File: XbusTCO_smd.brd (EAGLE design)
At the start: 54 x 70 mm, 80 parts, among them IC1 74HC4515D, IC2 PIC16F628P, IC3 MAX481CSA, IC4 78L05SMD, X1 1751264

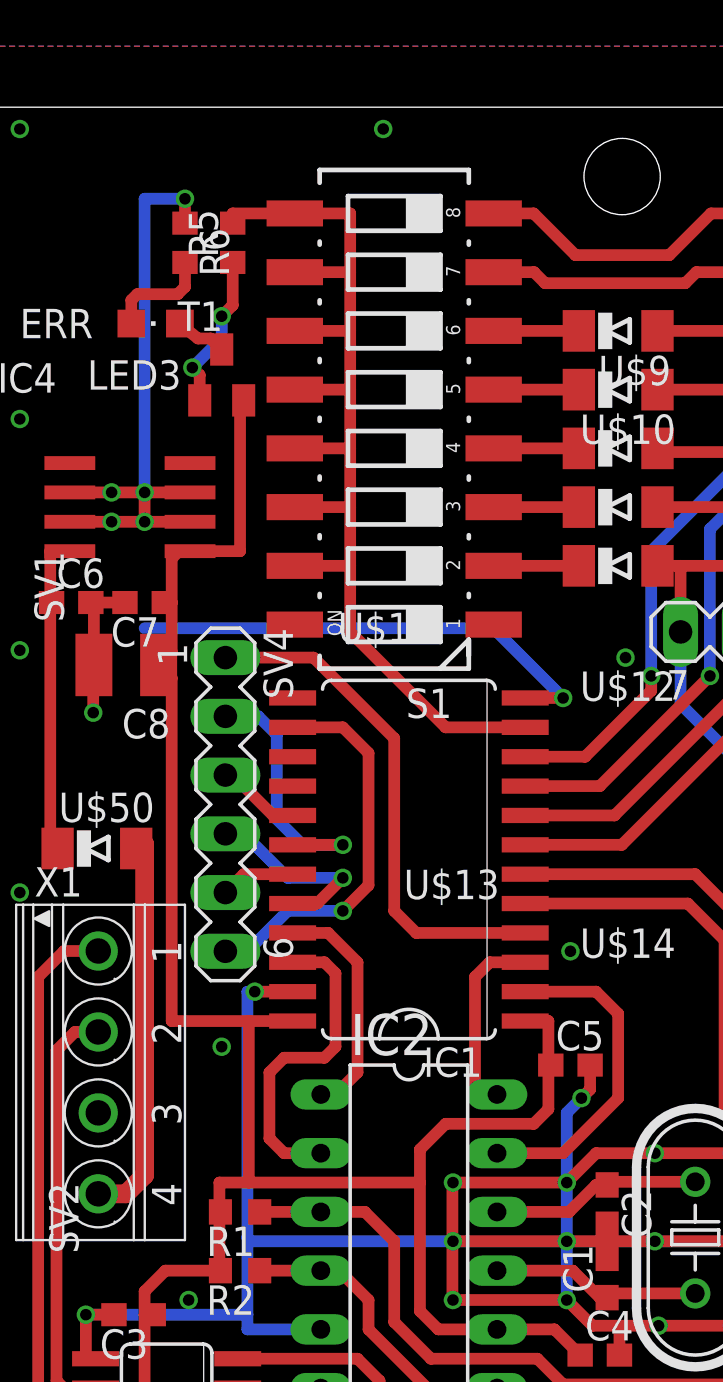
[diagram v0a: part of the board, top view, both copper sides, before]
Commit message: Updated DIL switch pinout.
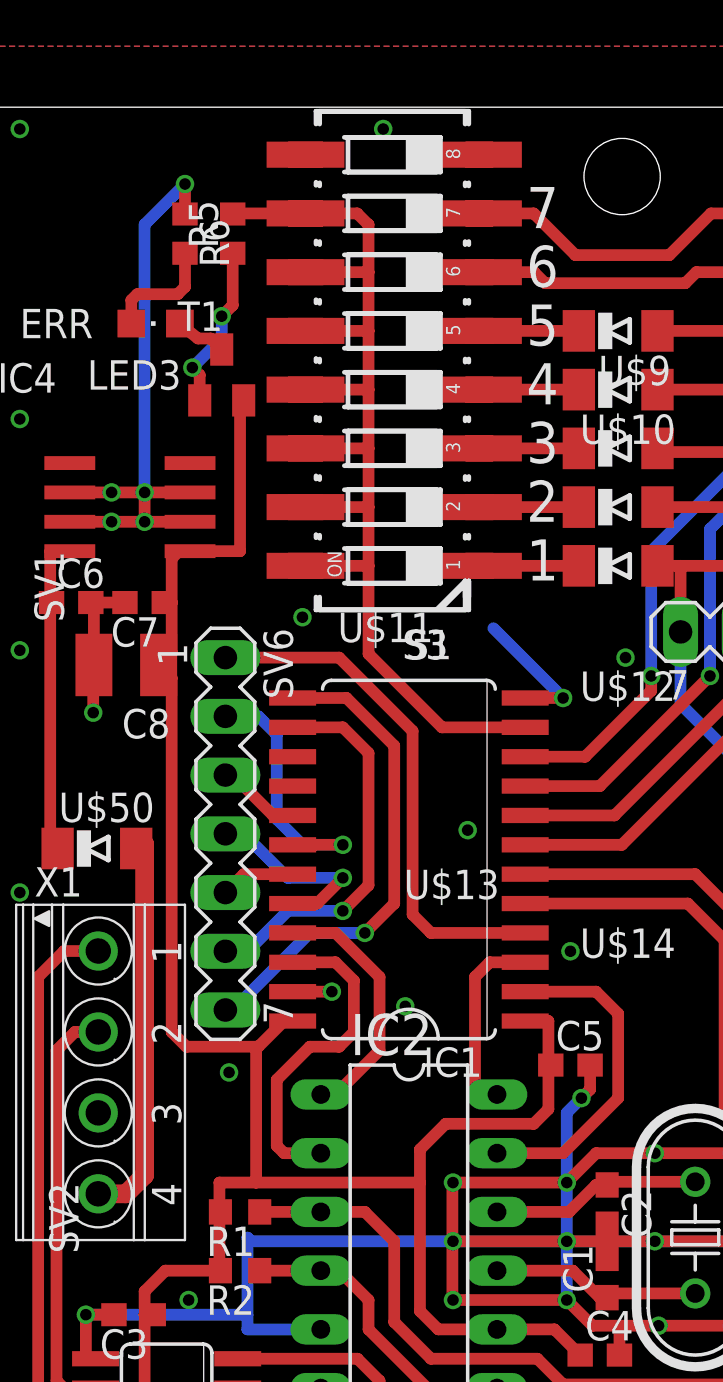
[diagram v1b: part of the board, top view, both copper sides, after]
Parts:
- removed SV4: (no value), con-lstb:MA06-1
- added S3: Farnel 1605476, switch-dil:CTS-219-08J
- added SV6: (no value), con-lstb:MA07-1
- moved S1 2.54 mm to (17.1, 59.1)
- moved R5 0.40 mm to (10.2, 64.5)
- moved R6 0.40 mm to (8.10, 64.5)
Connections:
- new net N$88: IC1.13, SV6.7
- net GND: now also S1.8, S1.9, S3.8, S3.9
- net N$30: now also S1.16, S3.10, S3.11, S3.12, S3.13, S3.14, S3.15, S3.16; no longer S1.9
- net N$31: now also S1.7, S3.7; no longer S1.8
- net N$32: now also S1.6, S3.6; no longer S1.7
- net N$33: now also S1.5, S3.5; no longer S1.6
- net N$34: now also S1.4, S3.4; no longer S1.5
- net N$35: now also S1.3, S3.3; no longer S1.4
- net N$36: now also S1.2, S3.2; no longer S1.3
- net N$37: now also S1.1, S3.1; no longer S1.2
- net N$82: now also SV6.1; no longer SV4.1
- net N$83: now also SV6.2; no longer SV4.2
- net N$84: now also SV6.3; no longer SV4.3
- net N$85: now also SV6.4; no longer SV4.4
- net N$86: now also SV6.5; no longer SV4.5
- net N$87: now also SV6.6; no longer SV4.6
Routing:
- net GND: track 172.1 -> 146.0 mm, vias 39 -> 42
- net N$88: track 0.00 -> 21.3 mm, vias 0 -> 1
- net N$30: track 47.2 -> 52.8 mm
- net N$32: track 12.5 -> 15.0 mm
- net N$37: track 3.68 -> 4.93 mm
- net N$36: track 3.68 -> 4.93 mm
- net N$35: track 3.68 -> 4.93 mm
- net N$34: track 3.68 -> 4.93 mm
- net N$33: track 3.68 -> 4.93 mm
- net N$31: track 13.6 -> 14.8 mm
- net N$5: track 10.1 -> 11.1 mm
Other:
- board text added: "1"
- board text added: "2"
- board text added: "3"
- board text added: "4"
- board text added: "5"
- board text added: "6"
- board text added: "7"

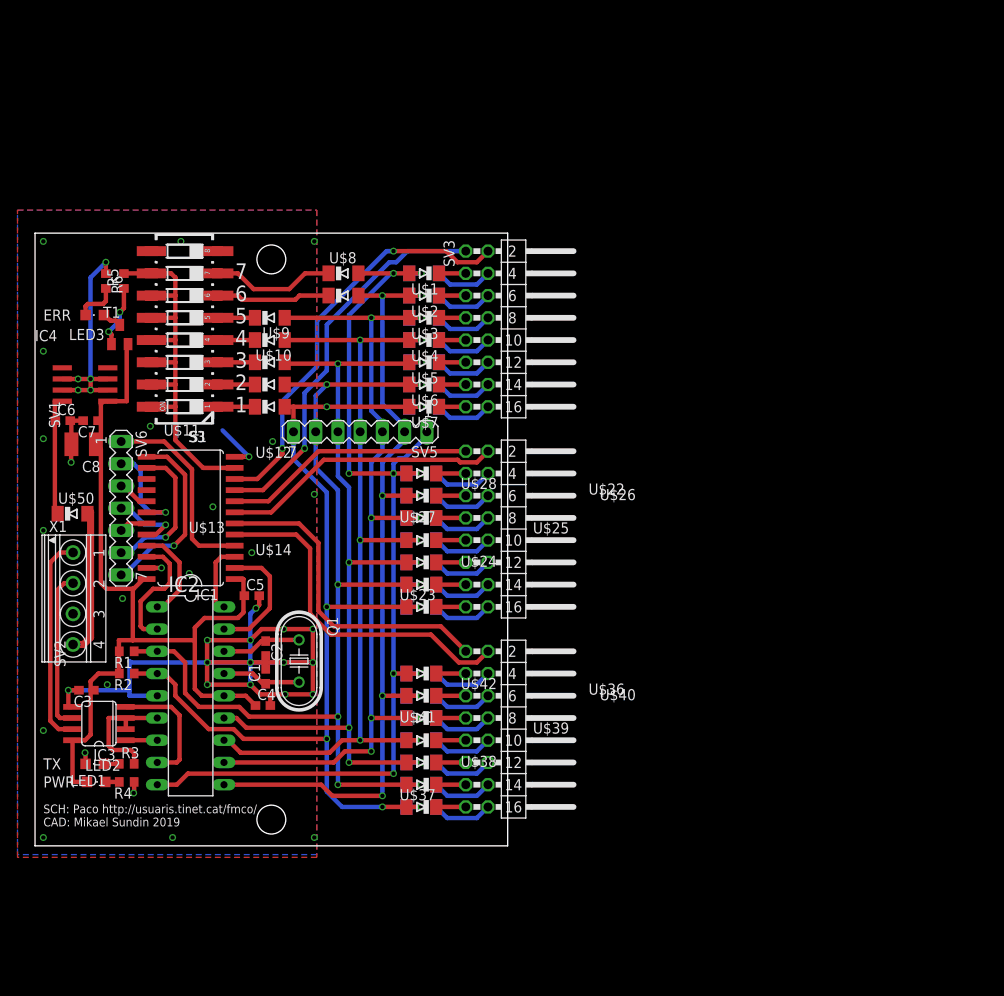
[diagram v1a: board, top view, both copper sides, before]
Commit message: Added 2 more connectors.
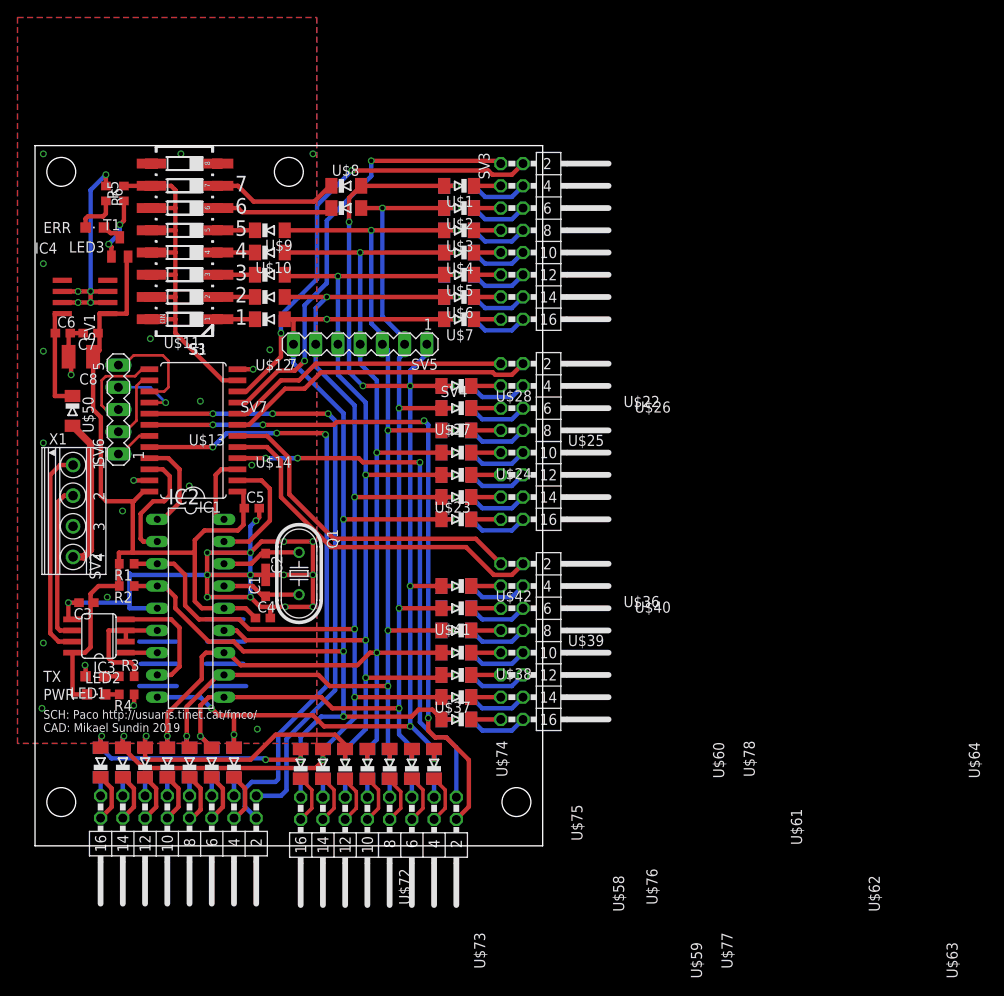
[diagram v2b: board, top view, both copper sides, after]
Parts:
- added SV4, SV7: (no value), con-lstb:MA08-2W
- added U$51, U$52, U$53, U$54, U$55, U$56, U$57, U$58, U$59, U$60, U$61, U$62, U$63, U$64, U$65, U$66, U$67, U$68, U$69, U$70, U$71, U$72, U$73, U$74, U$75, U$76, U$77, U$78: LL4148, LL4148:MINIMELF
- SV6: device con-lstb:MA07-1 -> con-lstb:MA05-1
- moved U$50 11.7 mm to (4.29, 49.7), turned to 270 degrees
- moved SV6 11.3 mm to (9.53, 49.8), turned to 90 degrees
- moved SV3 10.8 mm to (54.5, 69.1)
- moved U$17 10.8 mm to (48.5, 65.2)
- moved U$5 10.8 mm to (48.5, 65.2)
- moved SV1 10.8 mm to (54.5, 46.2)
- moved SV2 10.8 mm to (54.5, 23.3)
- moved U$1 10.8 mm to (48.5, 75.4)
- moved U$15 10.8 mm to (48.5, 60.2)
- moved U$16 10.8 mm to (48.5, 62.7)
- moved U$18 10.8 mm to (48.5, 67.8)
- moved U$19 10.8 mm to (48.5, 70.3)
- moved U$21 10.8 mm to (48.5, 75.4)
- moved U$22 10.8 mm to (48.1, 52.5)
- moved U$23 10.8 mm to (48.1, 50.0)
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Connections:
- new net N$100: SV4.7, U$53.C
- new net N$101: SV4.9, U$54.C
- new net N$102: SV4.11, U$55.C
- new net N$103: SV4.13, U$56.C
- new net N$104: SV4.15, U$57.C
- new net N$105: SV4.16, U$58.C
- new net N$106: SV4.14, U$59.C
- new net N$107: SV4.12, U$60.C
- new net N$108: SV4.10, U$61.C
- new net N$109: SV4.8, U$62.C
- new net N$110: SV4.6, U$63.C
- new net N$111: SV4.4, U$64.C
- new net N$112: SV7.7, U$67.C
- new net N$113: SV7.9, U$68.C
- new net N$114: SV7.11, U$69.C
- new net N$115: SV7.13, U$70.C
- new net N$116: SV7.15, U$71.C
- new net N$117: SV7.16, U$72.C
- new net N$118: SV7.14, U$73.C
- new net N$119: SV7.12, U$74.C
- new net N$120: SV7.10, U$75.C
- new net N$121: SV7.8, U$76.C
- new net N$122: SV7.6, U$77.C
- new net N$123: SV7.4, U$78.C
- new net N$89: IC1.16, SV6.4
- new net N$90: IC1.15, SV6.5
- new net N$96: SV7.3, U$65.C
- new net N$97: SV7.5, U$66.C
- new net N$98: SV4.3, U$51.C
- new net N$99: SV4.5, U$52.C
- net N$10: now also U$51.A, U$64.A, U$65.A, U$78.A
- net N$11: now also U$52.A, U$63.A, U$66.A, U$77.A
- net N$12: now also U$53.A, U$62.A, U$67.A, U$76.A
- net N$13: now also U$54.A, U$61.A, U$68.A, U$75.A
- net N$14: now also U$55.A, U$60.A, U$69.A, U$74.A
- net N$15: now also U$56.A, U$59.A, U$70.A, U$73.A
- net N$16: now also U$57.A, U$58.A, U$71.A, U$72.A
- net N$82: now also SV4.1; no longer SV6.1
- net N$83: now also SV4.2; no longer SV6.2
- net N$84: now also SV7.1; no longer SV6.3
- net N$85: now also SV7.2; no longer SV6.4
- net N$86: now also SV6.1; no longer SV6.5
- net N$87: now also SV6.2; no longer SV6.6
- net N$88: now also SV6.3; no longer SV6.7
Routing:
- net N$83: track 11.7 -> 80.6 mm, vias 1 -> 4
- net N$84: track 3.63 -> 69.8 mm, vias 0 -> 3
- net N$85: track 8.50 -> 70.7 mm, vias 1 -> 3
- net N$14: track 97.9 -> 150.4 mm, vias 7 -> 9
- net N$16: track 114.1 -> 162.4 mm, vias 7 -> 10
- net N$15: track 115.2 -> 163.0 mm, vias 7 -> 9
- net N$13: track 96.8 -> 138.3 mm, vias 6 -> 8
- net N$82: track 22.5 -> 61.8 mm, vias 0 -> 3
- net N$12: track 99.8 -> 134.5 mm, vias 7 -> 9
- net GND: track 146.0 -> 180.6 mm, vias 42 -> 40
- net N$11: track 98.7 -> 128.0 mm, vias 7 -> 9
- net N$10: track 117.1 -> 144.5 mm, vias 8 -> 11
- net N$90: track 0.00 -> 11.8 mm
- net N$88: track 21.3 -> 10.9 mm, vias 1 -> 0
- net N$87: track 16.8 -> 8.30 mm, vias 1 -> 0
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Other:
- board size 54 x 70 mm -> 58 x 80 mm

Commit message: Added pdf files, added smd component size in value field.
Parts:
- C1, C2: value (none) -> TBD/0603
- C6, C7: value 100n -> 100n/0603
- C8: value 47uF -> 47uF/1210
- IC3: value MAX481CSA -> MAX481CSA / SO8
- LED1, LED2, LED3: value (none) -> 0805
- Q1: value (none) -> 8Mhz
- R1, R2, R5: value 10k -> 10k/0603
- R3, R4, R6: value 1k2 -> 1k2/0603
